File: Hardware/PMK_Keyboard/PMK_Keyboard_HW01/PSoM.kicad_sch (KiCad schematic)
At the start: 1 part, among them J601 PSoM_ESP32S2_Carrier_Board

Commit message: Working on schematic
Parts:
- added R101, R102: R, symbol Component_lib:R
- added TH101: Thermistor_NTC, symbol Component_lib:NTCS0402E3473GXT
- renumbered J601 to J101
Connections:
- net D+: now also J101.56 (D+)
- net D-: now also J101.58 (D-)
- net GND: now also J101.1 (GND), J101.2 (GND), J101.22 (GND), J101.24 (GND), J101.41 (GND), J101.54 (GND), J101.59 (GND), J101.60 (GND), TH101.2
- net VBAT: now also J101.4 (VBAT), J101.6 (VBAT), J101.8 (VBAT)
- net VBUS: now also J101.10 (VBUS), J101.12 (VBUS)
- net PL: now reaches J101.11 (IO5)
- net VSYS: now reaches J101.14 (VSYS)
- net VSYS: now also J101.16 (VSYS)
- net SPI_CLK_ESP: now reaches J101.15 (IO7)
- net SPI_CLK_ESP: now also R102.1
- net +3V3: now reaches J101.18 (3V3)
- net +3V3: now also J101.20 (3V3)
- net CE: now reaches J101.19 (IO9)
- net GP_CE: now reaches J101.21 (IO10)
- net BATTERY_TEMP: now reaches J101.3 (BATTERY_TEMP)
- net BATTERY_TEMP: now also TH101.1
- net SPI_MISO: now reaches J101.7 (IO3)
- net SPI_MISO: now also R102.2
- net LED_MOSI: now reaches J101.9 (IO4)
- net LED_MOSI: now also R101.2
- new net LED_MOSI_ESP: R101.1

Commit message: Started routing
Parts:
- added J102: PSoM_ESP32S2_Carrier_Board, Component_lib:PSoM_ESP32S2_00, symbol Component_lib:PSoM_ESP32S2_Carrier_Board
- J101: footprint (none) -> Component_lib:PSoM_ESP32S2_00
- R101, R102, TH101: footprint (none) -> Resistor_SMD:R_0402_1005Metric
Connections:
- net +3V3: now also J102.18 (3V3), J102.20 (3V3)
- net BATTERY_TEMP: now also J102.3 (BATTERY_TEMP)
- net CE: now also J102.19 (IO9)
- net D+: now also J102.56 (D+)
- net D-: now also J102.58 (D-)
- net GND: now also J102.1 (GND), J102.2 (GND), J102.22 (GND), J102.24 (GND), J102.41 (GND), J102.54 (GND), J102.59 (GND), J102.60 (GND)
- net GP_CE: now also J102.21 (IO10)
- net LED_MOSI: now also J102.9 (IO4)
- net PL: now also J102.11 (IO5)
- net SPI_CLK_ESP: now also J102.15 (IO7)
- net SPI_MISO: now also J102.7 (IO3)
- net VBAT: now also J102.4 (VBAT), J102.6 (VBAT), J102.8 (VBAT)
- net VBUS: now also J102.10 (VBUS), J102.12 (VBUS)
- net VSYS: now also J102.14 (VSYS), J102.16 (VSYS)
- net SDA: now reaches J101.25 (IO12)
- net SDA: now also J102.25 (IO12)
- net SCL: now reaches J101.27 (IO13)
- net SCL: now also J102.27 (IO13)
- net INT: now reaches J101.29 (IO14)
- net INT: now also J102.29 (IO14)
- net SPI_MOSI: now reaches J101.5 (IO2)
- net SPI_MOSI: now also J102.5 (IO2)
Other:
- moved on the sheet: J101, R101, R102, TH101

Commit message: working on routing
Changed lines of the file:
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@@
+    (stroke (width 0) (type default))
+  )
+  (wire (pts (xy 271.78 106.68) (xy 274.32 106.68))
     (stroke (width 0) (type default))
   )
@@
     (stroke (width 0) (type default))
   )
+  (wire (pts (xy 271.78 111.76) (xy 274.32 111.76))
+    (stroke (width 0) (type default))
+  )
   (wire (pts (xy 271.78 35.56) (xy 274.32 35.56))
     (stroke (width 0) (type default))
@@
     (stroke (width 0) (type default))
   )
-  (wire (pts (xy 271.78 109.22) (xy 271.78 106.68))
+  (wire (pts (xy 271.78 119.38) (xy 271.78 116.84))
     (stroke (width 0) (type default))
   )
@@
     (stroke (width 0) (type default))
   )
-  (wire (pts (xy 271.78 106.68) (xy 274.32 106.68))
+  (wire (pts (xy 271.78 116.84) (xy 274.32 116.84))
     (stroke (width 0) (type default))
   )
@@
     (effects (font (size 1.27 1.27)) (justify left bottom))
   )
+  (label "A" (at 271.78 106.68 180) (fields_autoplaced)
+    (effects (font (size 1.27 1.27)) (justify right bottom))
+  )
   (label "SDA" (at 271.78 76.2 180) (fields_autoplaced)
     (effects (font (size 1.27 1.27)) (justify right bottom))
@@
     (effects (font (size 1.27 1.27)) (justify right bottom))
   )
+  (label "B" (at 271.78 111.76 180) (fields_autoplaced)
+    (effects (font (size 1.27 1.27)) (justify right bottom))
+  )
   (label "VBAT" (at 93.98 71.12 0) (fields_autoplaced)
     (effects (font (size 1.27 1.27)) (justify left bottom))
@@
     (effects (font (size 1.27 1.27)) (justify left))
   )
+  (hierarchical_label "B" (shape input) (at 274.32 111.76 0) (fields_autoplaced)
+    (effects (font (size 1.27 1.27)) (justify left))
+  )
   (hierarchical_label "INT" (shape input) (at 274.32 86.36 0) (fields_autoplaced)
     (effects (font (size 1.27 1.27)) (justify left))
@@
     (effects (font (size 1.27 1.27)) (justify left))
   )
-  (hierarchical_label "GND" (shape passive) (at 274.32 106.68 0) (fields_autoplaced)
+  (hierarchical_label "GND" (shape passive) (at 274.32 116.84 0) (fields_autoplaced)
     (effects (font (size 1.27 1.27)) (justify left))
   )
@@
   )
   (hierarchical_label "SDA" (shape bidirectional) (at 274.32 76.2 0) (fields_autoplaced)
+    (effects (font (size 1.27 1.27)) (justify left))
+  )
+  (hierarchical_label "A" (shape input) (at 274.32 106.68 0) (fields_autoplaced)
     (effects (font (size 1.27 1.27)) (justify left))
   )
@@
     )
   )
-  (symbol (lib_id "power:GND") (at 271.78 109.22 0) (unit 1)
+  (symbol (lib_id "power:GND") (at 271.78 119.38 0) (unit 1)
     (in_bom yes) (on_board yes) (dnp no) (fields_autoplaced)
-    (property "Reference" "#PWR0118" (at 271.78 115.57 0)
-      (effects (font (size 1.27 1.27)) hide)
-    )
-    (property "Value" "GND" (at 271.78 113.6634 0)
-      (effects (font (size 1.27 1.27)))
-    )
-    (property "Footprint" "" (at 271.78 109.22 0)
-      (effects (font (size 1.27 1.27)) hide)
-    )
-    (property "Datasheet" "" (at 271.78 109.22 0)
-      (effects (font (size 1.27 1.27)) hide)
-    )
+    (property "Reference" "#PWR0118" (at 271.78 125.73 0)
+      (effects (font (size 1.27 1.27)) hide)
+    )
+    (property "Value" "GND" (at 271.78 123.8234 0)
+      (effects (font (size 1.27 1.27)))
+    )
+    (property "Footprint" "" (at 271.78 119.38 0)
+      (effects (font (size 1.27 1.27)) hide)
+    )
+    (property "Datasheet" "" (at 271.78 119.38 0)
+      (effects (font (size 1.27 1.27)) hide)
+    )

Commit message: Need to route Shift registers
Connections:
- net A: now also J101.31 (IO15), J102.31 (IO15)
- net B: now also J101.33 (IO16), J102.33 (IO16)
- net LED_MOSI: no longer J101.9 (IO4), J102.9 (IO4)
- net LED_MOSI_ESP: now also J101.9 (IO4), J102.9 (IO4)
- net SPI_CLK: now also R102.2
- net SPI_MISO: no longer R102.2
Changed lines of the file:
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@@
   (junction (at 124.46 119.38) (diameter 0) (color 0 0 0 0)
   )
+  (wire (pts (xy 119.38 109.22) (xy 127 109.22))
+    (stroke (width 0) (type default))
+  )
   (wire (pts (xy 231.14 127) (xy 233.68 127))
     (stroke (width 0) (type default))
@@
     (stroke (width 0) (type default))
   )
+  (wire (pts (xy 119.38 106.68) (xy 127 106.68))
+    (stroke (width 0) (type default))
+  )
   (wire (pts (xy 119.38 93.98) (xy 127 93.98))
     (stroke (width 0) (type default))
@@
     (stroke (width 0) (type default))
   )
+  (wire (pts (xy 50.8 106.68) (xy 58.42 106.68))
+    (stroke (width 0) (type default))
+  )
   (wire (pts (xy 241.3 127) (xy 243.84 127))
     (stroke (width 0) (type default))
@@
   )
   (wire (pts (xy 124.46 142.24) (xy 127 142.24))
+    (stroke (width 0) (type default))
+  )
+  (wire (pts (xy 50.8 109.22) (xy 58.42 109.22))
     (stroke (width 0) (type default))
   )
@@
     (effects (font (size 1.27 1.27)) (justify right bottom))
   )
-  (label "LED_MOSI" (at 50.8 78.74 180) (fields_autoplaced)
+  (label "A" (at 119.38 106.68 180) (fields_autoplaced)
+    (effects (font (size 1.27 1.27)) (justify right bottom))
+  )
+  (label "B" (at 119.38 109.22 180) (fields_autoplaced)
     (effects (font (size 1.27 1.27)) (justify right bottom))
   )
@@
     (effects (font (size 1.27 1.27)) (justify right bottom))
   )
+  (label "SPI_CLK" (at 243.84 134.62 0) (fields_autoplaced)
+    (effects (font (size 1.27 1.27)) (justify left bottom))
+  )
   (label "INT" (at 50.8 104.14 180) (fields_autoplaced)
     (effects (font (size 1.27 1.27)) (justify right bottom))
@@
     (effects (font (size 1.27 1.27)) (justify right bottom))
   )
+  (label "B" (at 50.8 109.22 180) (fields_autoplaced)
+    (effects (font (size 1.27 1.27)) (justify right bottom))
+  )
   (label "PL" (at 119.38 81.28 180) (fields_autoplaced)
     (effects (font (size 1.27 1.27)) (justify right bottom))
@@
     (effects (font (size 1.27 1.27)) (justify left bottom))
   )
+  (label "A" (at 50.8 106.68 180) (fields_autoplaced)
+    (effects (font (size 1.27 1.27)) (justify right bottom))
+  )
+  (label "LED_MOSI_ESP" (at 119.38 78.74 180) (fields_autoplaced)
+    (effects (font (size 1.27 1.27)) (justify right bottom))
+  )
   (label "D-" (at 93.98 139.7 0) (fields_autoplaced)
     (effects (font (size 1.27 1.27)) (justify left bottom))
@@
     (effects (font (size 1.27 1.27)) (justify left bottom))
   )
-  (label "SPI_MISO" (at 243.84 134.62 0) (fields_autoplaced)
-    (effects (font (size 1.27 1.27)) (justify left bottom))
-  )
   (label "VBUS" (at 162.56 78.74 0) (fields_autoplaced)
     (effects (font (size 1.27 1.27)) (justify left bottom))
   )
-  (label "LED_MOSI" (at 119.38 78.74 180) (fields_autoplaced)
-    (effects (font (size 1.27 1.27)) (justify right bottom))
-  )
+  (label "LED_MOSI_ESP" (at 50.8 78.74 180) (fields_autoplaced)
+    (effects (font (size 1.27 1.27)) (justify right bottom))
+  )

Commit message: Need to add some silkscreenthen done!
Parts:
- added TH102: Thermistor_NTC, Resistor_SMD:R_0402_1005Metric, symbol Component_lib:NTCS0402E3473GXT
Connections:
- net BATTERY_TEMP: now also TH102.1
- net GND: now also TH102.2
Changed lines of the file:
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@@
+    (stroke (width 0) (type default))
+  )
+  (wire (pts (xy 198.12 93.98) (xy 200.66 93.98))
     (stroke (width 0) (type default))
   )
@@
     (stroke (width 0) (type default))
   )
+  (wire (pts (xy 200.66 93.98) (xy 200.66 96.52))
+    (stroke (width 0) (type default))
+  )
   (wire (pts (xy 55.88 119.38) (xy 55.88 142.24))
     (stroke (width 0) (type default))
   )
-  (wire (pts (xy 271.78 119.38) (xy 271.78 116.84))
+  (wire (pts (xy 271.78 124.46) (xy 271.78 121.92))
     (stroke (width 0) (type default))
   )
@@
     (stroke (width 0) (type default))
   )
+  (wire (pts (xy 269.24 116.84) (xy 271.78 116.84))
+    (stroke (width 0) (type default))
+  )
   (wire (pts (xy 88.9 96.52) (xy 86.36 96.52))
     (stroke (width 0) (type default))
@@
     (stroke (width 0) (type default))
   )
-  (wire (pts (xy 271.78 116.84) (xy 274.32 116.84))
+  (wire (pts (xy 271.78 121.92) (xy 274.32 121.92))
     (stroke (width 0) (type default))
   )
@@
   )
   (wire (pts (xy 231.14 104.14) (xy 231.14 106.68))
+    (stroke (width 0) (type default))
+  )
+  (wire (pts (xy 200.66 104.14) (xy 200.66 106.68))
     (stroke (width 0) (type default))
   )
@@
     (effects (font (size 1.27 1.27)) (justify right bottom))
   )
+  (label "BATTERY_TEMP" (at 198.12 93.98 180) (fields_autoplaced)
+    (effects (font (size 1.27 1.27)) (justify right bottom))
+  )
   (label "A" (at 119.38 106.68 180) (fields_autoplaced)
     (effects (font (size 1.27 1.27)) (justify right bottom))
@@
     (effects (font (size 1.27 1.27)) (justify left bottom))
   )
+  (label "GP_CE" (at 269.24 116.84 180) (fields_autoplaced)
+    (effects (font (size 1.27 1.27)) (justify right bottom))
+  )
   (label "SCL" (at 119.38 101.6 180) (fields_autoplaced)
     (effects (font (size 1.27 1.27)) (justify right bottom))
@@
     (effects (font (size 1.27 1.27)) (justify left))
   )
-  (hierarchical_label "GND" (shape passive) (at 274.32 116.84 0) (fields_autoplaced)
+  (hierarchical_label "GND" (shape passive) (at 274.32 121.92 0) (fields_autoplaced)
     (effects (font (size 1.27 1.27)) (justify left))
   )
@@
   )
   (hierarchical_label "+3V3" (shape input) (at 274.32 45.72 0) (fields_autoplaced)
+    (effects (font (size 1.27 1.27)) (justify left))
+  )
+  (hierarchical_label "GP_CE" (shape input) (at 271.78 116.84 0) (fields_autoplaced)
     (effects (font (size 1.27 1.27)) (justify left))
   )
@@
     )
   )
-  (symbol (lib_id "power:GND") (at 271.78 119.38 0) (unit 1)
-    (in_bom yes) (on_board yes) (dnp no) (fields_autoplaced)
-    (property "Reference" "#PWR0118" (at 271.78 125.73 0)
-      (effects (font (size 1.27 1.27)) hide)
-    )
-    (property "Value" "GND" (at 271.78 123.8234 0)
-      (effects (font (size 1.27 1.27)))
-    )
-    (property "Footprint" "" (at 271.78 119.38 0)
-      (effects (font (size 1.27 1.27)) hide)
-    )
-    (property "Datasheet" "" (at 271.78 119.38 0)
+  (symbol (lib_id "power:GND") (at 271.78 124.46 0) (unit 1)
+    (in_bom yes) (on_board yes) (dnp no) (fields_autoplaced)
+    (property "Reference" "#PWR0118" (at 271.78 130.81 0)
+      (effects (font (size 1.27 1.27)) hide)
+    )
+    (property "Value" "GND" (at 271.78 128.9034 0)
+      (effects (font (size 1.27 1.27)))
+    )
+    (property "Footprint" "" (at 271.78 124.46 0)
+      (effects (font (size 1.27 1.27)) hide)
+    )
+    (property "Datasheet" "" (at 271.78 124.46 0)
       (effects (font (size 1.27 1.27)) hide)
     )
@@
     )
   )
+  (symbol (lib_id "Component_lib:NTCS0402E3473GXT") (at 200.66 101.6 0) (unit 1)
+    (in_bom yes) (on_board yes) (dnp no) (fields_autoplaced)
+    (property "Reference" "TH102" (at 203.073 100.0038 0)
+      (effects (font (size 1.27 1.27)) (justify left))
+    )
+    (property "Value" "Thermistor_NTC" (at 203.073 101.9248 0)
+      (effects (font (size 1.27 1.27)) (justify left))
+    )
+    (property "Footprint" "Resistor_SMD:R_0402_1005Metric" (at 200.66 99.06 0)
+      (effects (font (size 1.27 1.27)) hide)
+    )
+    (property "Datasheet" "https://www.mouser.ch/ProductDetail/Vishay-BC-Components/NTCS0402E3473GXT?qs=8wHch9UpSva8flR6dht9RA%3D%3D" (at 200.66 99.06 0)
+      (effects (font (size 1.27 1.27)) hide)
+    )
+    (pin "1")
+    (pin "2")
+    (instances
+      (project "PMK_Keyboard_HW01"
+        (path "/c3b08055-08a5-4979-9bf8-f36ab0917722/f4bd3789-d94c-4771-8f5c-2a22000e96d6"
+          (reference "TH102") (unit 1)
+        )
+      )
+    )
+  )
   (symbol (lib_id "Component_lib:NTCS0402E3473GXT") (at 231.14 101.6 0) (unit 1)
     (in_bom yes) (on_board yes) (dnp no) (fields_autoplaced)
@@
         )
       )
+    )
+  )
+  (symbol (lib_id "power:GND") (at 200.66 106.68 0) (unit 1)
+    (in_bom yes) (on_board yes) (dnp no) (fields_autoplaced)
+    (property "Reference" "#PWR0118" (at 200.66 113.03 0)
+      (effects (font (size 1.27 1.27)) hide)
+    )
+    (property "Value" "GND" (at 200.66 111.1234 0)
+      (effects (font (size 1.27 1.27)))
+    )
+    (property "Footprint" "" (at 200.66 106.68 0)
+      (effects (font (size 1.27 1.27)) hide)
+    )
+    (property "Datasheet" "" (at 200.66 106.68 0)
+      (effects (font (size 1.27 1.27)) hide)
+    )
+    (pin "1")
+    (instances
+      (project "PMK_Keyboard_HW01"
+        (path "/c3b08055-08a5-4979-9bf8-f36ab0917722/cf9fd53d-a626-44ae-9c40-26b02d8cda14"
+          (reference "#PWR0118") (unit 1)
+        )
+        (path "/c3b08055-08a5-4979-9bf8-f36ab0917722/f4bd3789-d94c-4771-8f5c-2a22000e96d6"
+          (reference "#PWR0323") (unit 1)
+        )
+      )

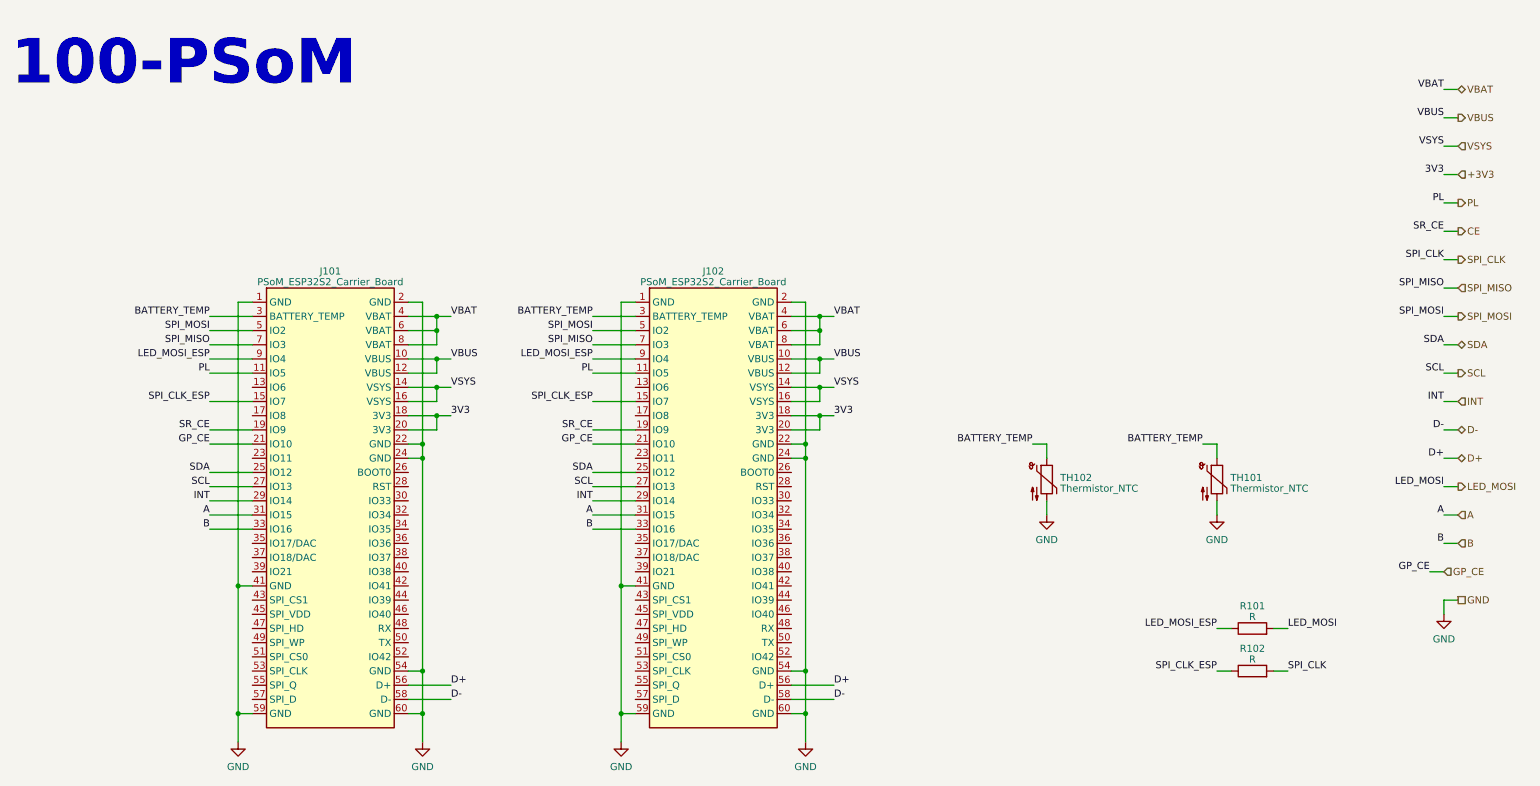
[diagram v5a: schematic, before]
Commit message: added mounting holes + fix in ref des
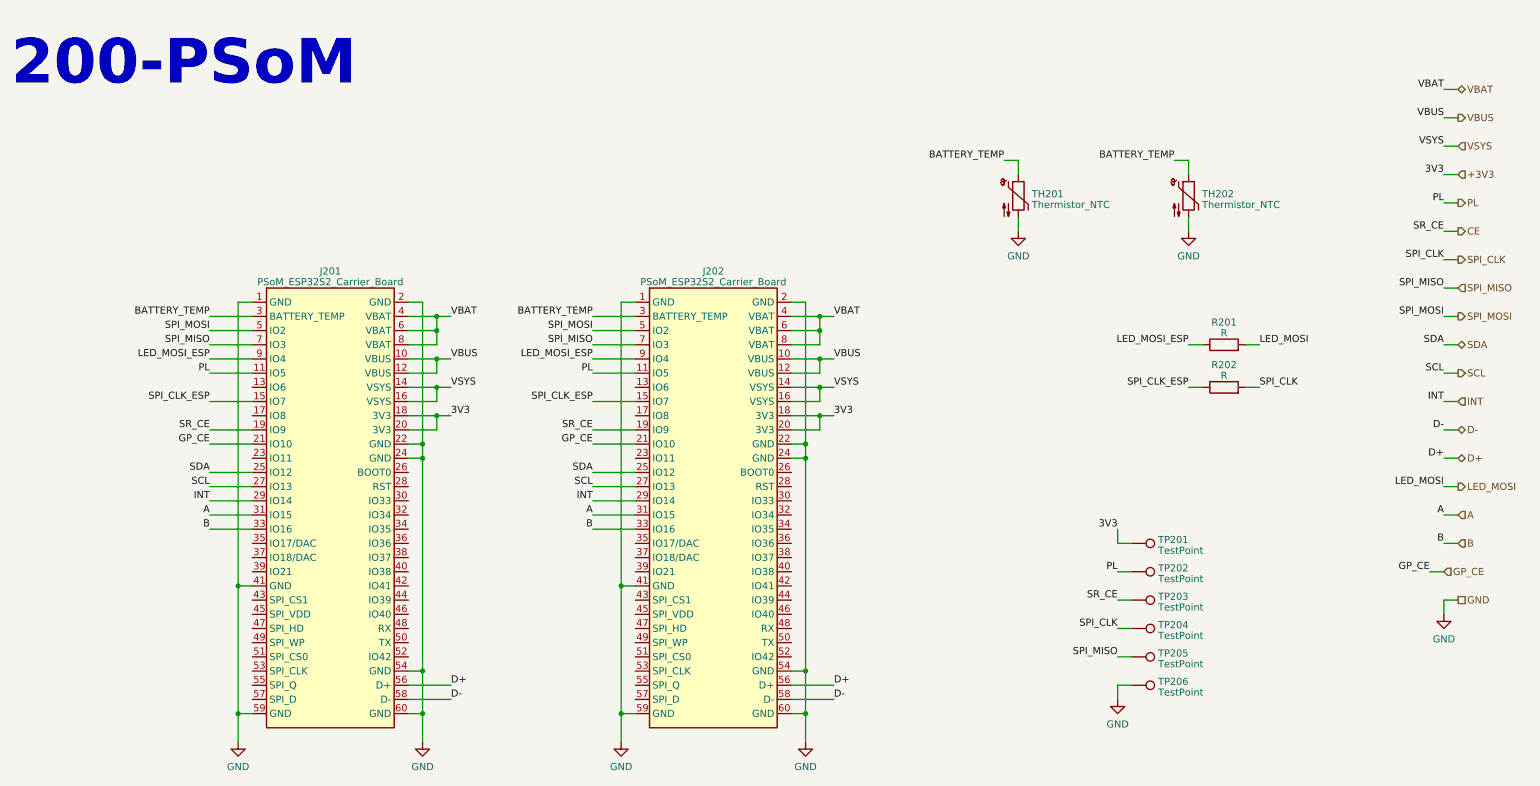
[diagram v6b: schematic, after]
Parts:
- added TP201, TP202, TP203, TP204, TP205, TP206: TestPoint, TestPoint:TestPoint_Pad_D1.5mm, symbol Connector:TestPoint
- renumbered J101 to J201, J102 to J202, R101 to R201, R102 to R202, TH102 to TH201, TH101 to TH202
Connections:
- net +3V3: now also TP201.1
- net CE: now also TP203.1
- net GND: now also TP206.1
- net PL: now also TP202.1
- net SPI_CLK: now also TP204.1
- net SPI_MISO: now also TP205.1
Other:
- note added: "200-PSoM"
- note removed: "100-PSoM"
- moved on the sheet: R201, R202, TH201, TH202
